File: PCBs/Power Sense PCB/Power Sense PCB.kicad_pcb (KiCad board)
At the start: 2 copper layers, 84 parts, among them J1 Jack-DC, J10 Test Conn, J2 PWR_INV, J3 PWR_INPUT, J4 PHASE_A_INV, J5 PHASE_A_MOTOR, J6 PHASE_B_INV, J7 PHASE_B_MOTOR, J8 PHASE_C_INV, J9 PHASE_C_MOTOR, U1 INA240A1D, U2 INA240A1D, U3 INA240A1D, U4 INA240A1D

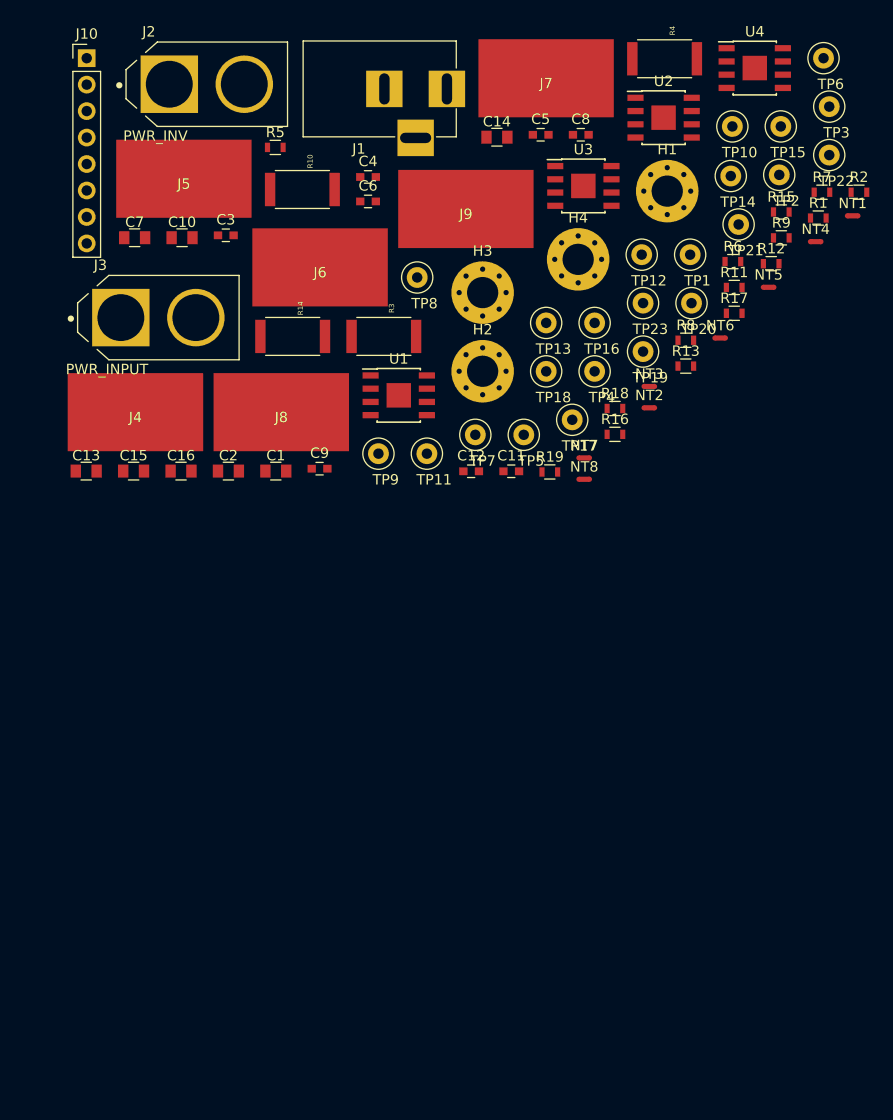
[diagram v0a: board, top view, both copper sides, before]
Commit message: Layout + Routing
- Added 5V LED indicatior
- Added 330uF bulk cap on 5V rail
- Changed 8pin to 9pin header (added ground)
- Completed all layout and routing!
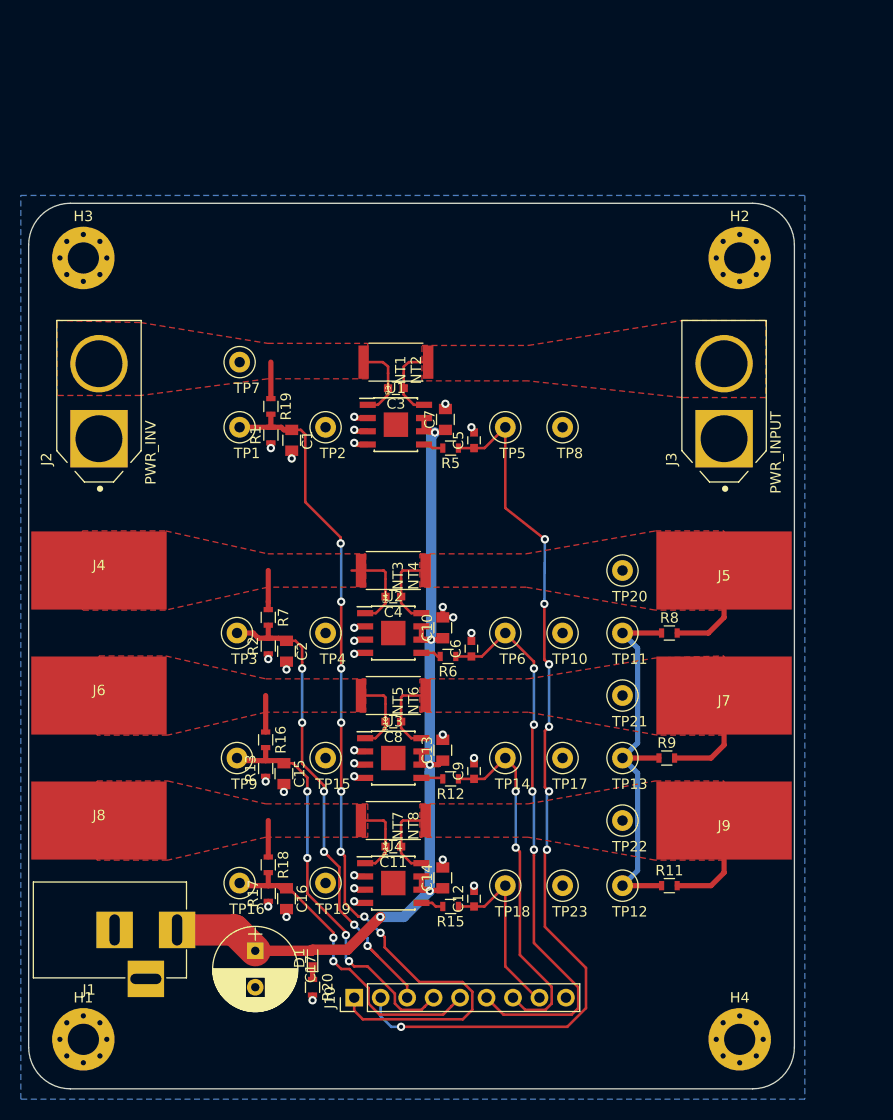
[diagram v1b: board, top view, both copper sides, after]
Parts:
- added C17: 330uF, Capacitors_THT:CP_Radial_D8.0mm_P3.50mm, F.Cu at (77.0, 112.5)
- added D1: RED, LEDs:LED_0603, F.Cu at (82.5, 113.2)
- added R20: 330, Resistors_SMD:R_0603, F.Cu at (82.5, 116.0)
- J10: footprint Pin_Headers:Pin_Header_Straight_1x08_Pitch2.54mm -> Pin_Headers:Pin_Header_Straight_1x09_Pitch2.54mm
- NT1, NT2, NT3, NT4, NT5, NT6, NT7, NT8: footprint NetTies:NetTie-2_SMD_Pad0.5mm -> Power Sense PCB:NetTie-2_SMD_Pad0.25mm
- moved H1 98.8 mm to (60.5, 121.0)
- moved J10 93.8 mm to (86.5, 117.0), turned to 90 degrees
- moved U4 85.6 mm to (90.2, 106.0)
- moved J1 84.8 mm to (69.5, 110.5)
- moved H4 76.5 mm to (123.5, 121.0)
- moved TP3 76.1 mm to (75.2, 82.0)
- moved TP15 74.7 mm to (83.8, 94.0)
- moved R15 73.8 mm to (95.8, 108.2), turned to 180 degrees
- moved R2 71.5 mm to (78.2, 83.2), turned to 90 degrees
- moved R17 71.4 mm to (78.2, 107.0), turned to 90 degrees
- moved C14 71.3 mm to (95.0, 105.5), turned to 90 degrees
- moved R7 67.0 mm to (78.2, 80.5), turned to 270 degrees
- moved TP22 66.9 mm to (112.2, 100.0)
- moved J5 64.0 mm to (122.0, 76.0)
- moved J9 63.7 mm to (122.0, 100.0)
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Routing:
- net /I_BUS: track 0.00 -> 87.9 mm, vias 0 -> 7
- net /V_BUS: track 0.00 -> 85.8 mm, vias 0 -> 8
- net +5V: track 0.00 -> 85.3 mm, vias 0 -> 5
- net /I_PHASE_A: track 0.00 -> 54.4 mm, vias 0 -> 4
- net /V_PHASE_A: track 0.00 -> 47.2 mm, vias 0 -> 6
- net /V_PHASE_B: track 0.00 -> 39.2 mm, vias 0 -> 4
- net /MOTOR_NEUTRAL: track 0.00 -> 37.7 mm
- net /I_PHASE_B: track 0.00 -> 35.2 mm, vias 0 -> 2
- net /V_PHASE_C: track 0.00 -> 31.3 mm, vias 0 -> 2
- net GND: track 0.00 -> 25.6 mm, vias 0 -> 30
- net /I_PHASE_C: track 0.00 -> 17.6 mm
- net /PHASE_C_MOTOR: track 0.00 -> 12.4 mm
- net /PHASE_B_MOTOR: track 0.00 -> 12.4 mm
- net /PHASE_A_MOTOR: track 0.00 -> 12.0 mm
- net Net-(J4-Pad1): track 0.00 -> 7.07 mm
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- added copper zone on F.Cu, net /PHASE_A_MOTOR
- added copper zone on F.Cu, net /PHASE_B_MOTOR
- added copper zone on F.Cu, net /PHASE_C_MOTOR
- added copper zone on B.Cu, net GND
- added copper zone on F.Cu, net Net-(J2-Pad2)
- added copper zone on F.Cu, net Net-(J3-Pad2)
- added copper zone on F.Cu, net Net-(J4-Pad1)
- added copper zone on F.Cu, net Net-(J6-Pad1)
- added copper zone on F.Cu, net Net-(J8-Pad1)
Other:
- board outline added: 73.5 x 85 mm

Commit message: Gerbers and Small Changes
- Swapped Ref1 and Ref2 values based on datasheet (doesn't matter really)
- Updated Silkscreen
- Exported Gerbers
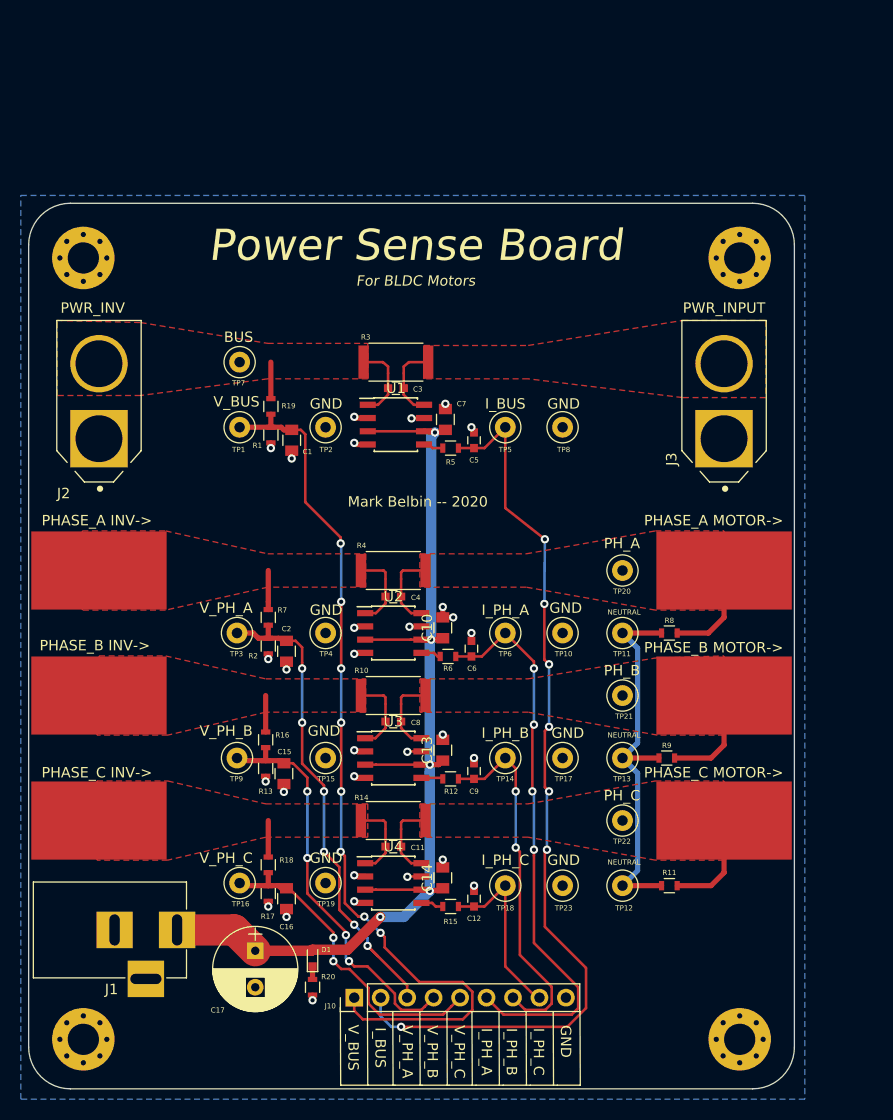
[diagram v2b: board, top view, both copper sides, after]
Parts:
- U1, U2, U3, U4: footprint Housings_SOIC:SOIC-8-1EP_3.9x4.9mm_Pitch1.27mm -> Housings_SOIC:SOIC-8_3.9x4.9mm_Pitch1.27mm
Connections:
- J1 pad 3: (no net) -> GND
- U1 pad 3: GND -> +5V
- U1 pad 7: +5V -> GND
- U2 pad 3: GND -> +5V
- U2 pad 7: +5V -> GND
- U3 pad 3: GND -> +5V
- U3 pad 7: +5V -> GND
- U4 pad 3: GND -> +5V
- U4 pad 7: +5V -> GND
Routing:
- net +5V: track 85.3 -> 101.8 mm
- net Net-(J4-Pad1): track 7.07 -> 6.17 mm
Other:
- board text added: "BUS"
- board text added: "For BLDC Motors"
- board text added: "GND"
- board text added: "I_BUS"
- board text added: "I_PH_A"
- board text added: "I_PH_B"
- board text added: "I_PH_C"
- board text added: "Mark Belbin -- 2020"
- board text added: "NEUTRAL"
- board text added: "PHASE_A INV->"
- board text added: "PHASE_A MOTOR->"
- board text added: "PHASE_B INV->"
- board text added: "PHASE_B MOTOR->"
- board text added: "PHASE_C INV->"
- board text added: "PHASE_C MOTOR->"
- board text added: "PH_A"
- board text added: "PH_B"
- board text added: "PH_C"
- board text added: "Power Sense Board"
- board text added: "V_BUS"
- board text added: "V_PH_A"
- board text added: "V_PH_B"
- board text added: "V_PH_C"
